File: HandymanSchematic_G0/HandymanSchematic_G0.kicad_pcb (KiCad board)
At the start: 4 copper layers, 104 parts, among them J1 SWD Header, J2 PWR, J3 JACKS, J4 FOOTSWITCH, J5 ScopeGroundLoop, Q1 BC847, Q2 BC847, Q3 2N7002, Q4 2N7002, SW1 RST, SW2 BYP, U1 TL074, U2 TL074, U3 TL072, U4 STM32G030F6P6, U5 AMS1117, U6 SSD1306, Y1 32.768kHZ

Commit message: control/encoder layout
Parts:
- moved D11 264.3 mm to (-1.95, 64.5)
- moved D10 263.7 mm to (-1.93, 55.0)
- moved SW2 217.3 mm to (-0.55, 36.6)
- moved J2 211.4 mm to (38.5, 25.4), turned to -90 degrees
- moved J3 210.7 mm to (33.3, 71.2), turned to -90 degrees
- moved J4 206.5 mm to (42.1, 71.3), turned to 90 degrees
- moved RV1 153.1 mm to (72.2, 25.4), turned to 180 degrees
- moved U6 140.3 mm to (5.65, 24.7)
- moved RV2 137.5 mm to (54.3, 25.3), turned to 180 degrees
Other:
- board outline added: 86 x 54 mm

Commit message: analog side layout
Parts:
- C1, C10, C11, C12, C13, C14, C15, C16, C17, C18, C19, C2, C20, C21, C22, C23, C24, C25, C3, C4, C5, C6, C7, C8, C9, D1, D2, D3, D4, D5, D6, D7, D8, D9, J1, J5, Q1, Q2, Q3, Q4, R1, R10, R11, R12, R13, R14, R15, R16, R17, R18, R19, R2, R20, R21, R22, R23, R24, R25, R26, R27, R28, R29, R3, R30, R31, R32, R33, R34, R35, R36, R37, R4, R5, R6, R7, R8, R9, SW1, TP1, TP10, TP11, TP2, TP3, TP4, TP5, TP6, TP7, TP8, TP9, U1, U2, U3, U4, U5, Y1: moved to B.Cu
- moved C10 150.1 mm to (45.0, 29.4), turned to 180 degrees
- moved C12 146.1 mm to (49.5, 32.6), turned to -90 degrees
- moved D1 145.7 mm to (63.6, 43.4), turned to 180 degrees
- moved D2 145.5 mm to (63.7, 46.0)
- moved U1 144.6 mm to (59.8, 37.0), turned to 90 degrees
- moved D3 141.7 mm to (66.0, 31.8), turned to -90 degrees
- moved C5 136.4 mm to (53.4, 39.2), turned to 90 degrees
- moved C1 134.8 mm to (53.5, 46.5), turned to -90 degrees
- moved R17 131.2 mm to (49.4, 29.4), turned to 180 degrees
- moved R23 130.0 mm to (54.1, 30.0), turned to 90 degrees
- moved C4 128.9 mm to (60.1, 42.5), turned to -90 degrees
- moved R22 128.4 mm to (54.1, 33.6), turned to 90 degrees
- moved C9 126.2 mm to (68.3, 31.8), turned to -90 degrees
- moved R16 124.7 mm to (57.2, 26.1), turned to 90 degrees
- moved C6 124.0 mm to (66.9, 36.2), turned to 90 degrees
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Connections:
- C5 pad 1: Net-(U1C-+) -> Net-(U1B-+)
- R7 pad 2: Net-(U1C-+) -> Net-(U1B-+)
- R8 pad 1: Net-(U1C-+) -> Net-(U1B-+)
- U1 pad 10: Net-(U1C-+) -> /Analog/Env
- U1 pad 5: /Analog/Env -> Net-(U1B-+)
- U1 pad 6: /Analog/Thresh -> /Analog/VG
- U1 pad 7: Net-(R22-Pad1) -> /Analog/VG
- U1 pad 8: /Analog/VG -> Net-(R22-Pad1)
- U1 pad 9: /Analog/VG -> /Analog/Thresh

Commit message: rough layout
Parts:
- removed TP8: 3v3, TestPoint:TestPoint_THTPad_D2.0mm_Drill1.0mm_VAL
- C11, C2, C3, C7, C8, D4, D5, D6, D7, Q1, Q2, Q3, Q4, R10, R11, R12, R14, R18, R19, R2, R20, R21, R32, R33, R34, R35, R4, R6, R9, U2: moved to F.Cu
- TP1: value AC -> AK
- moved R31 261.3 mm to (-0.55, 39.5), turned to 90 degrees
- moved R33 260.1 mm to (-4.25, 58.8), turned to -90 degrees
- moved R35 255.3 mm to (-3.83, 48.8), turned to -90 degrees
- moved R32 253.9 mm to (2.56, 67.5), turned to 90 degrees
- moved R34 253.0 mm to (2.88, 57.6), turned to 90 degrees
- moved SW1 249.2 mm to (19.3, 63.2), turned to 0 degrees
- moved U4 243.5 mm to (14.4, 50.0)
- moved R29 241.2 mm to (19.2, 59.2)
- moved D8 240.0 mm to (6.35, 66.5), turned to -90 degrees
- moved R30 239.1 mm to (21.2, 52.8)
- moved J1 232.0 mm to (6.45, 71.2), turned to -90 degrees
- moved R37 229.9 mm to (22.4, 36.1)
- moved Q3 229.7 mm to (1.56, 62.8)
- moved R36 228.0 mm to (24.4, 32.7)
- moved Q4 227.9 mm to (1.89, 52.8)
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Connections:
- R11 pad 1: Net-(U2C--) -> Net-(U2B--)
- R18 pad 2: Net-(U2B--) -> Net-(U2D--)
- R19 pad 2: Net-(U2D--) -> Net-(U2C--)
- R20 pad 1: Net-(U2B--) -> Net-(U2D--)
- R21 pad 1: Net-(U2D--) -> Net-(U2C--)
- R9 pad 2: Net-(U2C--) -> Net-(U2B--)
- U2 pad 14: Net-(C11-Pad1) -> /Analog/AmpAnode
- U2 pad 7: /Analog/AmpAnode -> Net-(R11-Pad2)
- U2 pad 8: Net-(R11-Pad2) -> Net-(C11-Pad1)

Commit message: routed & DRC passing
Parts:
- moved C8 2.82 mm to (53.7, 59.3)
- moved J5 2.32 mm to (38.8, 64.7)
- moved C23 0.25 mm to (41.0, 49.9)
- moved R32 0.20 mm to (2.55, 67.7)
- moved C20 0.07 mm to (34.0, 49.8)
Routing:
- net +3.3V: track 0.00 -> 167.8 mm, vias 0 -> 3
- net +9V: track 0.00 -> 153.7 mm, vias 0 -> 6
- net /Analog/VG: track 0.00 -> 130.2 mm, vias 0 -> 5
- net VCC: track 0.00 -> 68.1 mm, vias 0 -> 2
- net OPEN_IN: track 0.00 -> 63.5 mm, vias 0 -> 1
- net CLOSED_OUT: track 0.00 -> 56.3 mm
- net /Analog/SumPt: track 0.00 -> 55.6 mm, vias 0 -> 2
- net LOOP_OUT: track 0.00 -> 48.9 mm, vias 0 -> 1
- net GND: track 0.00 -> 43.2 mm, vias 0 -> 31
- net /Digital/TunerModeIn: track 0.00 -> 43.2 mm, vias 0 -> 2
- net FX_IN: track 0.00 -> 42.7 mm
- net LOOP_IN: track 0.00 -> 32.1 mm, vias 0 -> 1
- net /Analog/Thresh: track 0.00 -> 31.4 mm
- net SWDIO: track 0.00 -> 28.8 mm
- net SWCLK: track 0.00 -> 28.2 mm
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- added copper zone on In1.Cu, net GND
- added copper zone on In2.Cu, net GND

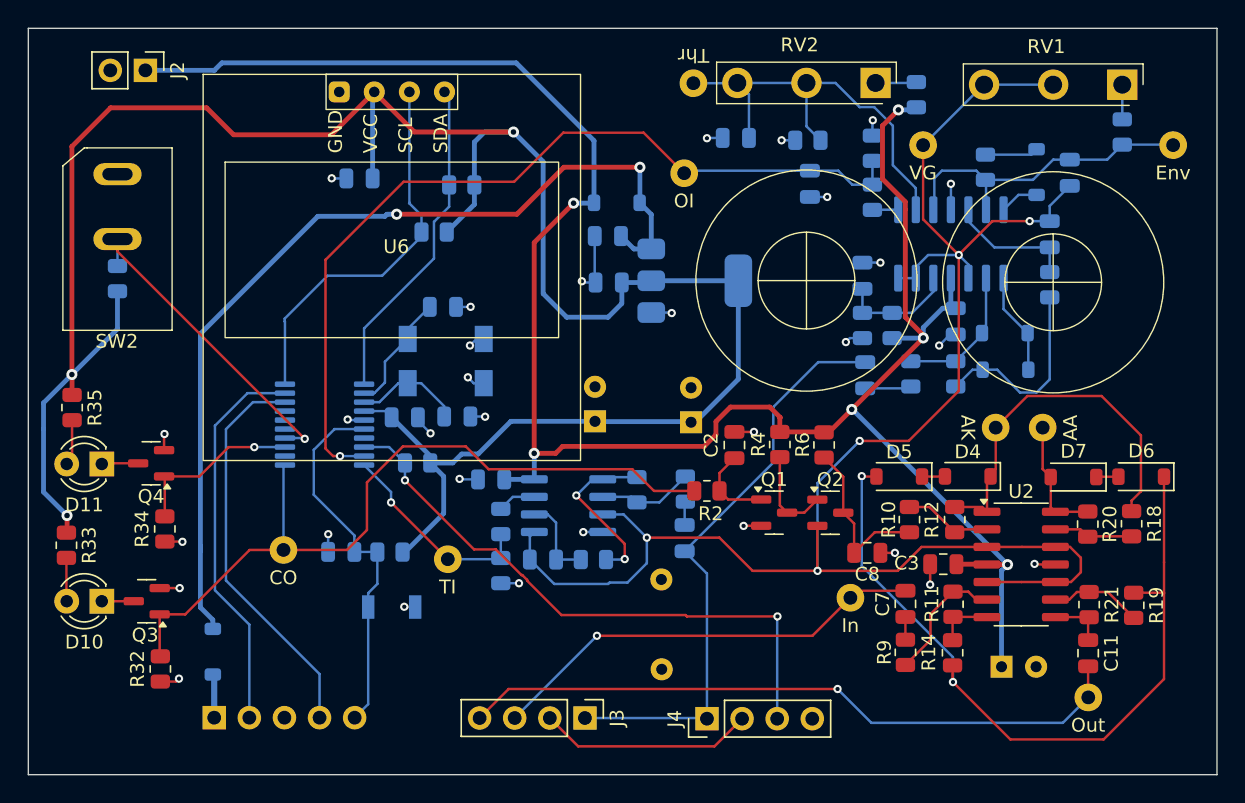
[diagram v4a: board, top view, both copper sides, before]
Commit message: silkscreen and stitching vias
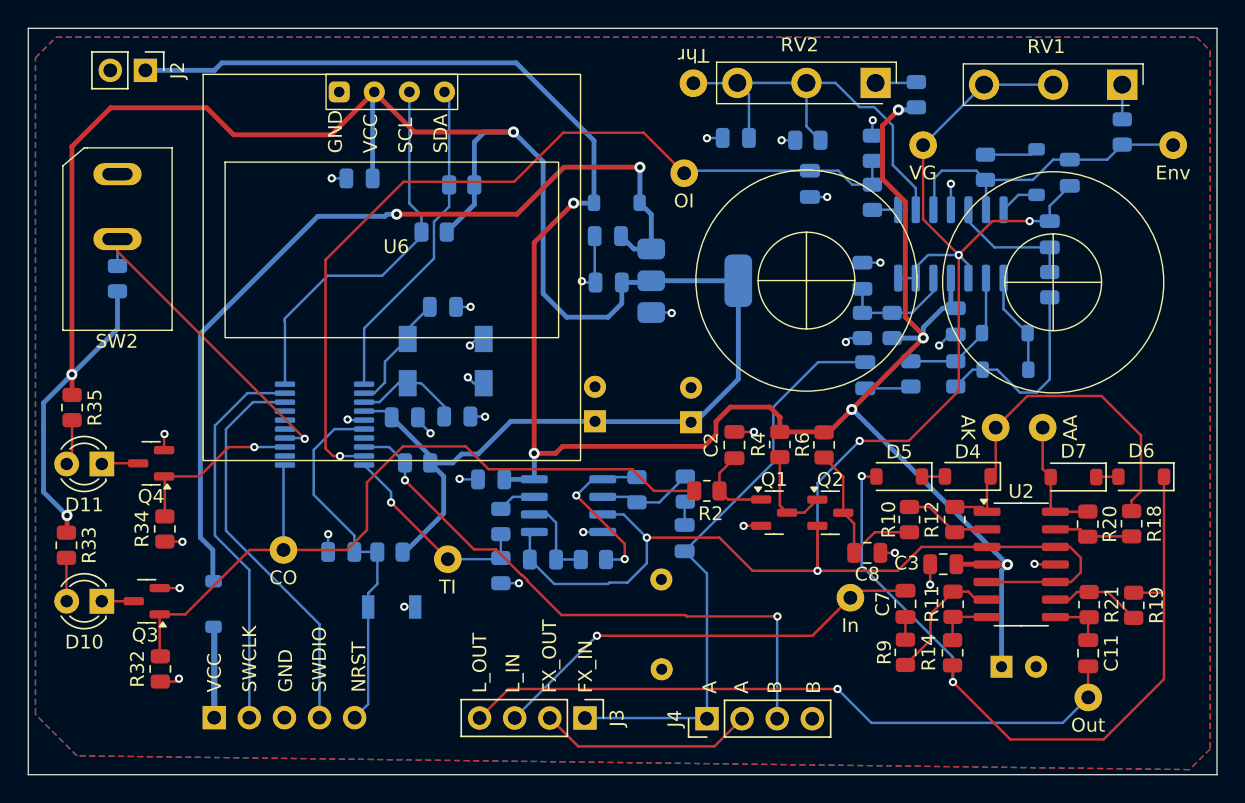
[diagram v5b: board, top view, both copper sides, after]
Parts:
- moved D8 3.45 mm to (6.40, 63.0)
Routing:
- net VCC: track 68.1 -> 63.9 mm
- net Net-(D8-A): track 3.17 -> 6.60 mm
- added copper zone on B.Cu, net GND
- added copper zone on F.Cu, net GND
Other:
- board text added: "A"
- board text added: "B"
- board text added: "FX_IN"
- board text added: "FX_OUT"
- board text added: "GND"
- board text added: "Handyman v1"
- board text added: "L_IN"
- board text added: "L_OUT"
- board text added: "NRST"
- board text added: "Rev. 1 - Feb 2025 Hayden Setlik"
- board text added: "SWCLK"
- board text added: "SWDIO"
- board text added: "VCC"

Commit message: rev1 ready for fab
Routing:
- net GND: vias 31 -> 201
